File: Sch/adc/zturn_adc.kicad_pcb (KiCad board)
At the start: 4 copper layers, 91.5 x 80 mm, 118 parts, among them CN1 SMA, CN2 SMA, CN3 AudioJack, J1 JP4, J2 Header5, J3 JP2, J4 JP2, J5 JP2, J6 JP2, P1 CONN_02X40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

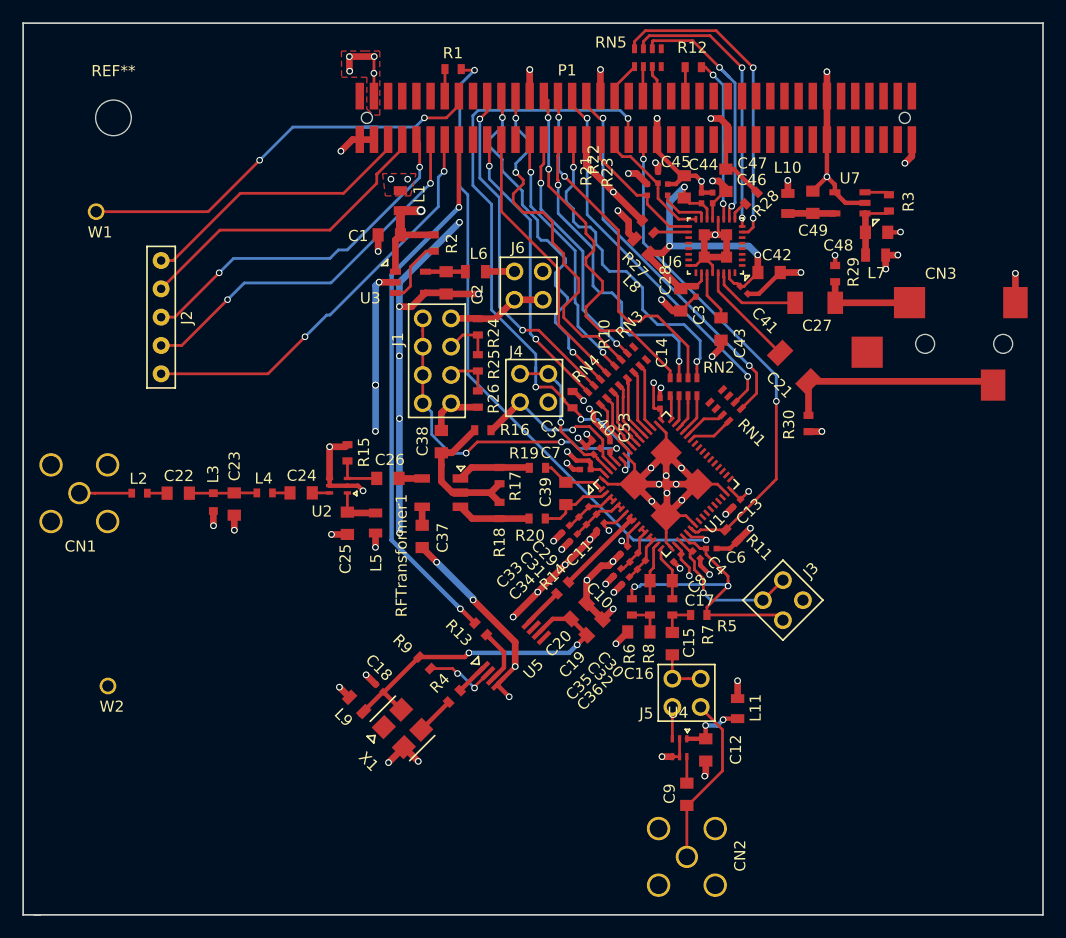
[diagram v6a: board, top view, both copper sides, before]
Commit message: Fixed C0603/1206 footprint
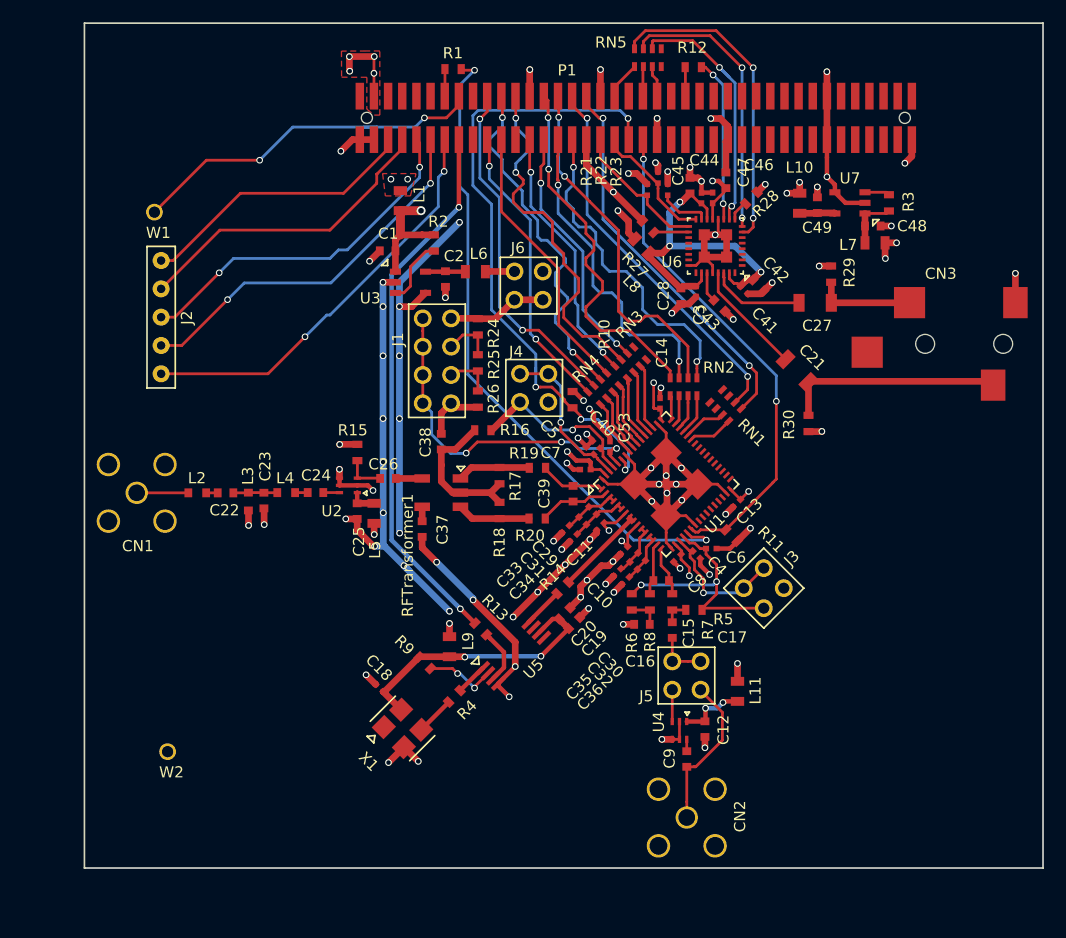
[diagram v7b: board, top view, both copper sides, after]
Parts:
- removed REF**: MountingHole_3.2mm_M3, Mounting_Holes:MountingHole_3.2mm_M3
- moved L9 9.81 mm to (124.3, 110.9), turned to 90 degrees
- moved W2 7.96 mm to (99.0, 120.4)
- moved W1 5.23 mm to (97.8, 72.0)
- moved L2 5.18 mm to (101.6, 97.1)
- moved CN1 5.15 mm to (96.2, 97.1)
- moved C22 4.24 mm to (104.2, 97.1)
- moved CN2 3.53 mm to (145.5, 126.3)
- moved C9 3.16 mm to (145.5, 121.0)
- moved L3 3.14 mm to (106.2, 97.9)
- moved C23 2.68 mm to (107.6, 97.8)
- moved C43 2.10 mm to (148.5, 80.3), turned to 315 degrees
- moved J3 2.03 mm to (152.4, 105.7)
- moved L4 1.93 mm to (109.6, 97.1)
- moved C19 1.89 mm to (135.4, 108.8)
- moved C12 1.87 mm to (147.2, 118.3)
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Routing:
- net Net-(C18-Pad1): track 31.3 -> 24.9 mm
- net /CN/VDDIO_13_PL: track 39.3 -> 34.1 mm
- net /RF_in/VCMB: track 26.1 -> 22.6 mm
- net Net-(C28-Pad1): track 33.7 -> 31.3 mm
- net GND: track 278.2 -> 280.3 mm, vias 73 -> 84
- net Net-(C22-Pad1): track 6.10 -> 3.96 mm
- net Net-(C25-Pad2): track 4.38 -> 2.48 mm
- net /AudioDAC/VREF: track 4.57 -> 2.72 mm
- net Net-(C4-Pad1): track 14.1 -> 12.3 mm
- net Net-(C9-Pad2): track 15.6 -> 14.0 mm
- net Net-(C9-Pad1): track 2.37 -> 1.06 mm
- net Net-(C48-Pad1): track 6.00 -> 4.88 mm
- net Net-(C49-Pad1): track 4.22 -> 3.19 mm
- net Net-(C15-Pad1): track 3.22 -> 2.33 mm
- net Net-(C21-Pad1): track 9.50 -> 10.3 mm
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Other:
- board size 91.5 x 80 mm -> 86 x 75.8 mm

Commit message: Reviewed footprint for C0402/L0603
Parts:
- moved C34 0.89 mm to (135.8, 100.4)
- moved C33 0.81 mm to (135.2, 99.8)
- moved C31 0.46 mm to (136.5, 99.3)
- moved C35 0.42 mm to (139.7, 104.1)
- moved C36 0.41 mm to (140.3, 104.7)
- moved R6 0.25 mm to (140.9, 106.9)
- moved C32 0.20 mm to (140.9, 103.5)
- moved C13 0.09 mm to (150.1, 98.0)
- moved L3 0.08 mm to (106.2, 97.8)
- moved C29 0.08 mm to (137.1, 98.7)
- moved C4 0.06 mm to (146.4, 102.7)
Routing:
- net GND: track 280.3 -> 276.2 mm, vias 84 -> 88
- net VDD3: track 23.5 -> 22.3 mm
- net Net-(C29-Pad2): track 5.24 -> 4.51 mm
- net Net-(C29-Pad1): track 5.10 -> 4.50 mm
